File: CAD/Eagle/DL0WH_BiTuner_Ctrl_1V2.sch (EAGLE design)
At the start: 157 parts, among them Q0321 ABS07-32.768KHZ, U0101 STM32L476RXT_64PIN_LDO, U0601 MC33996, U0701 MC33996, U0801 MC33996, U0921 TS5A23166, U0941 LM2611, U0951 OPA354, U0961 OPA354, U0962 MCP4661-103E-MS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

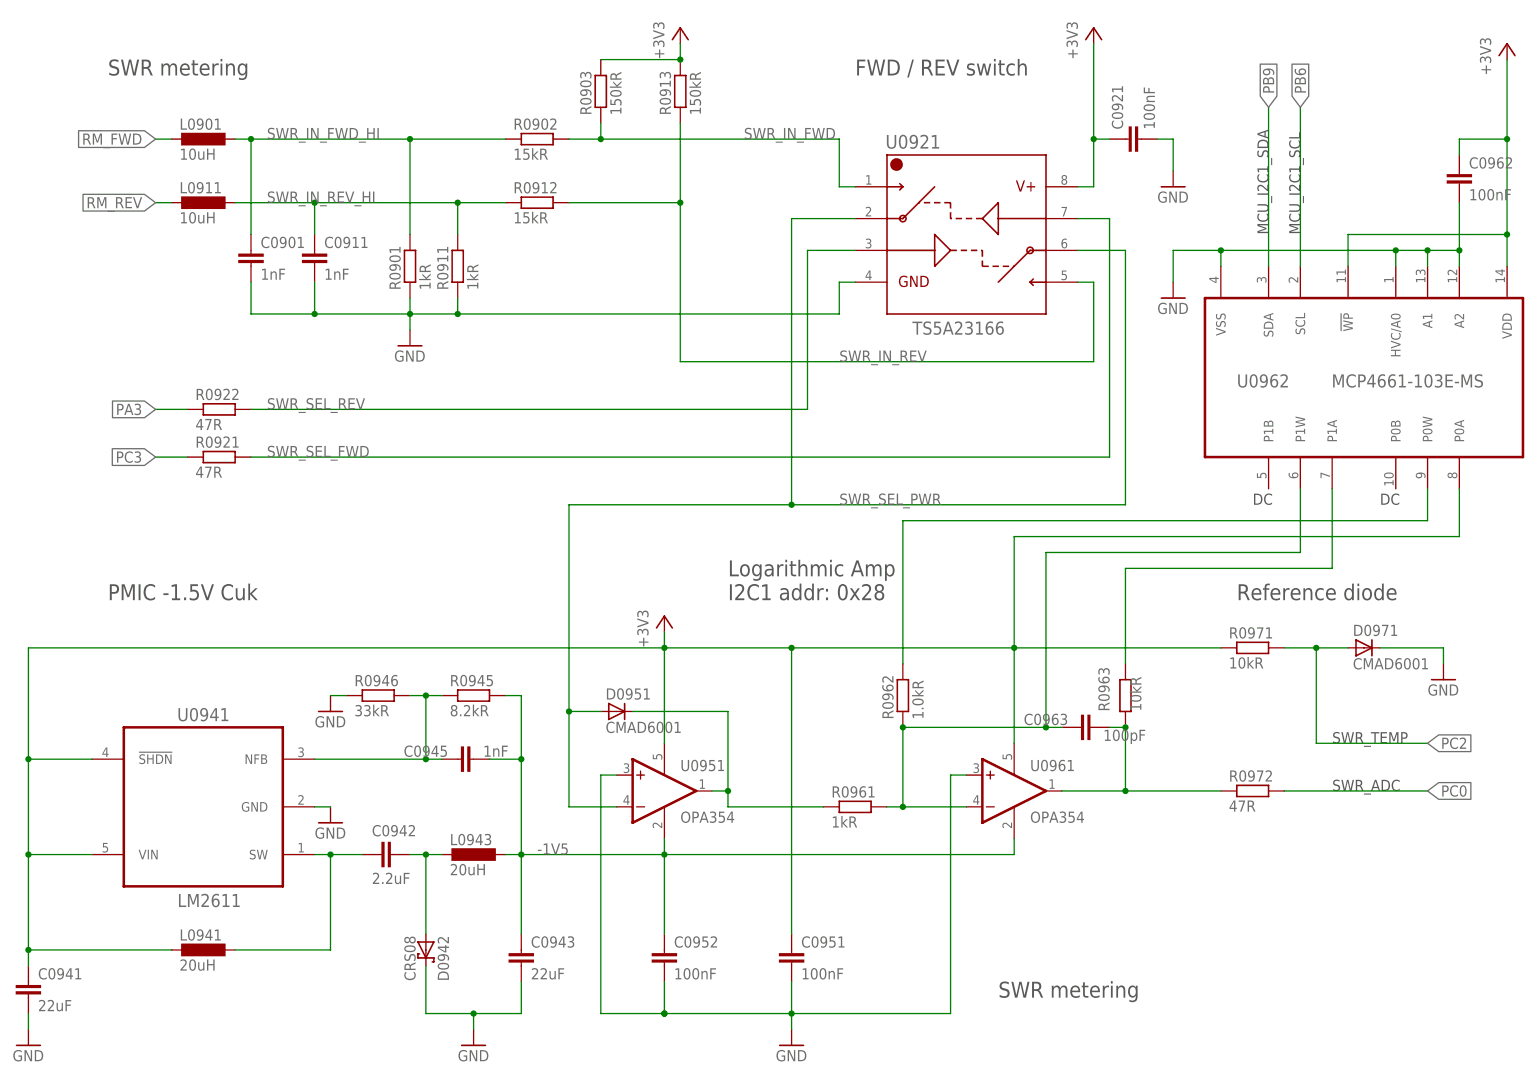
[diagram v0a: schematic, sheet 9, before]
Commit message: HW_1V2,HW_1V3 - CAD/Eagle - voltage divider added to tolerate voltages 0V..10V
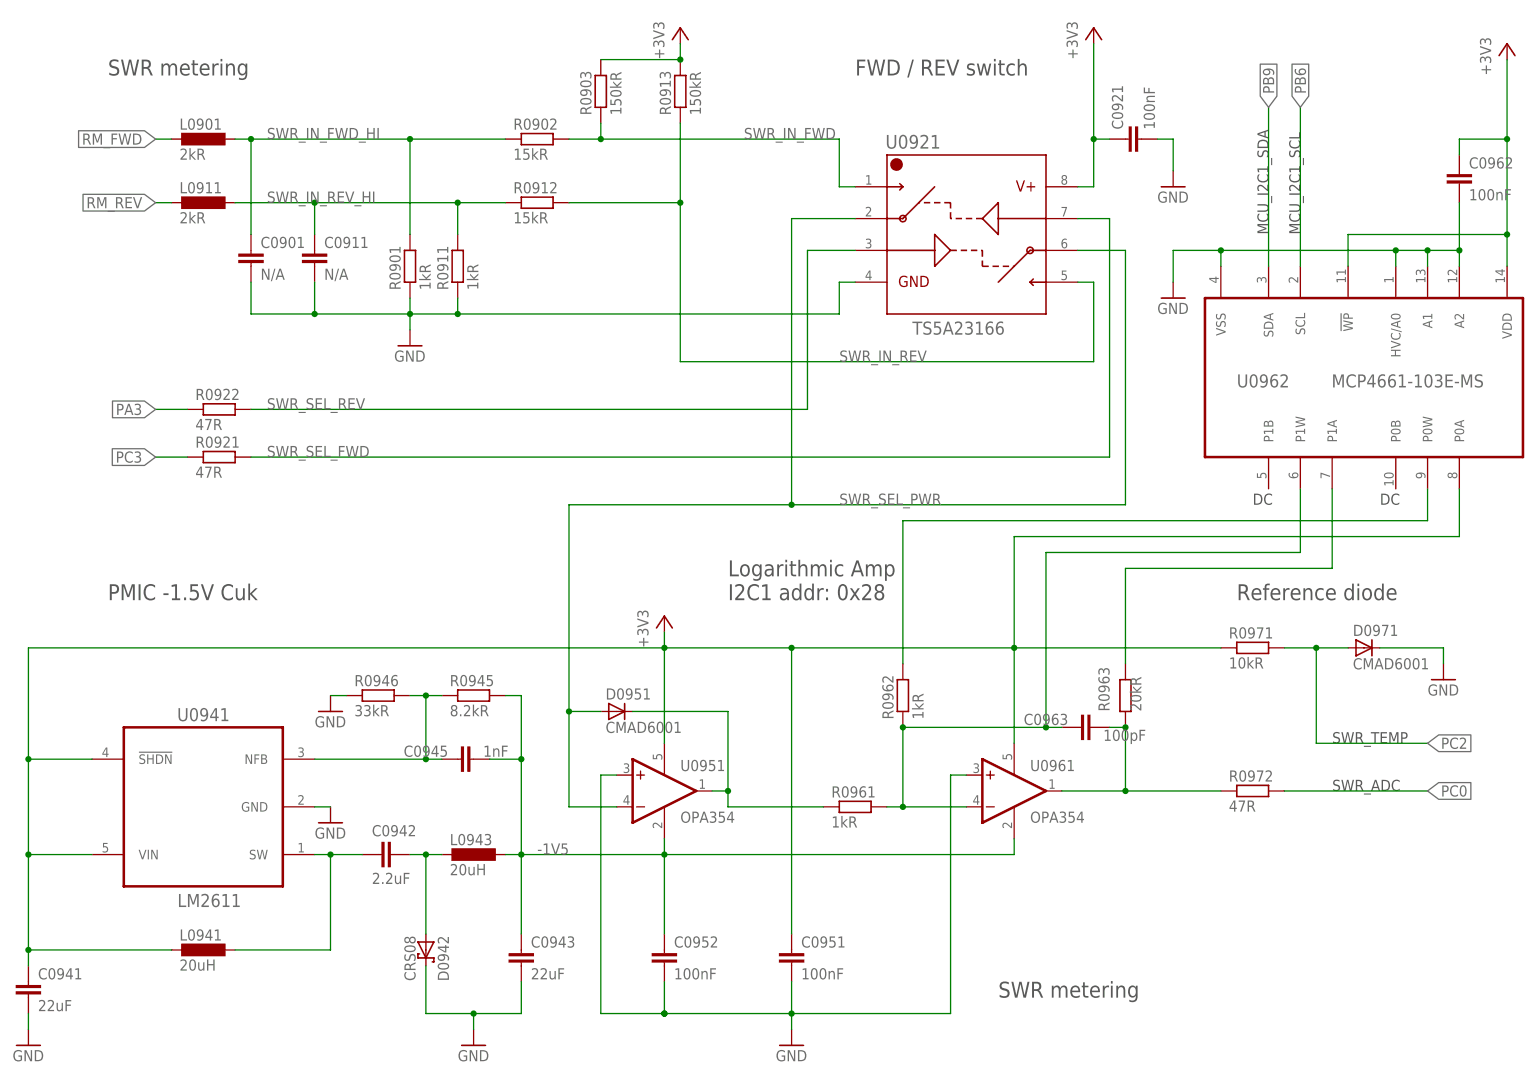
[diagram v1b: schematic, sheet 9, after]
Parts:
- C0901, C0911: value 1nF -> N/A
- L0901, L0911: value 10uH -> 2kR
- R0962: value 1.0kR -> 1kR
- R0963: value 10kR -> 20kR
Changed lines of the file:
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@@
 <part name="R1302" library="df4iah_rcl" deviceset="R-EU_" device="R0402" value="220kR"/>
 <part name="FRAME_05" library="df4iah_frame" deviceset="A4L-LOC" device="" value="Holes"/>
-<part name="L0901" library="df4iah_rcl" deviceset="L-EU" device="L0603" value="10uH"/>
-<part name="L0911" library="df4iah_rcl" deviceset="L-EU" device="L0603" value="10uH"/>
-<part name="C0901" library="df4iah_rcl" deviceset="C-EU" device="C0402" value="1nF"/>
-<part name="C0911" library="df4iah_rcl" deviceset="C-EU" device="C0402" value="1nF"/>
+<part name="L0901" library="df4iah_rcl" deviceset="L-EU" device="L0603" value="2kR"/>
+<part name="L0911" library="df4iah_rcl" deviceset="L-EU" device="L0603" value="2kR"/>
+<part name="C0901" library="df4iah_rcl" deviceset="C-EU" device="C0402" value="N/A"/>
+<part name="C0911" library="df4iah_rcl" deviceset="C-EU" device="C0402" value="N/A"/>
 <part name="R0912" library="df4iah_rcl" deviceset="R-EU_" device="R0402" value="15kR"/>
 <part name="R0902" library="df4iah_rcl" deviceset="R-EU_" device="R0402" value="15kR"/>
@@
 <part name="U0961" library="df4iah_opamp" deviceset="OPA354" device=""/>
 <part name="R0961" library="df4iah_rcl" deviceset="R-EU_" device="R0402" value="1kR"/>
-<part name="R0962" library="df4iah_rcl" deviceset="R-EU_" device="R0402" value="1.0kR"/>
-<part name="R0963" library="df4iah_rcl" deviceset="R-EU_" device="R0402" value="10kR"/>
+<part name="R0962" library="df4iah_rcl" deviceset="R-EU_" device="R0402" value="1kR"/>
+<part name="R0963" library="df4iah_rcl" deviceset="R-EU_" device="R0402" value="20kR"/>
 <part name="C0963" library="df4iah_rcl" deviceset="C-EU" device="C0402" value="100pF"/>
 <part name="U0941" library="df4iah_powersupply" deviceset="LM2611" device=""/>
